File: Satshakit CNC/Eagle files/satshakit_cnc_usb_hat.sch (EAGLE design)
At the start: 30 parts

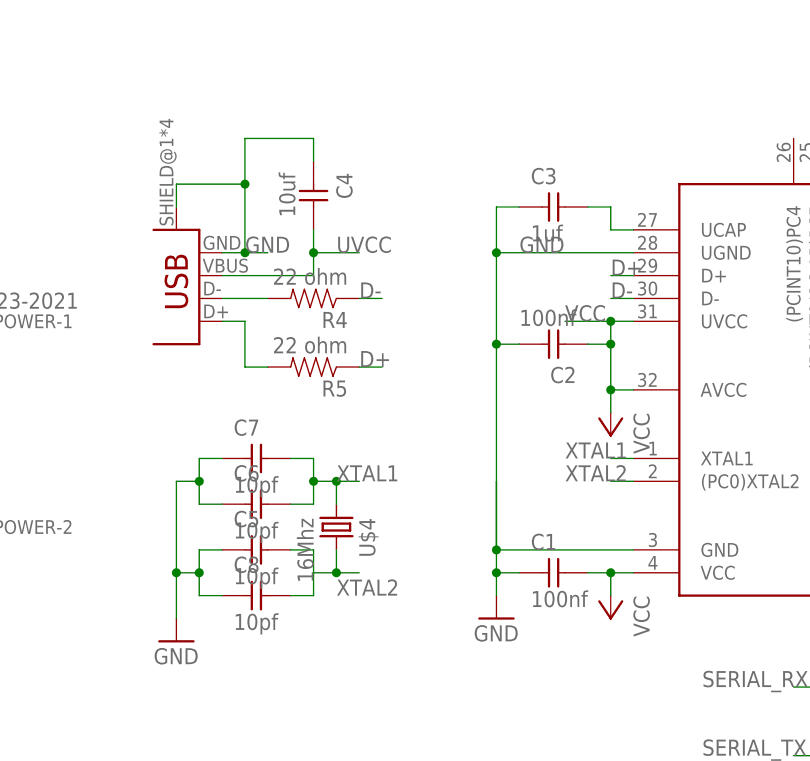
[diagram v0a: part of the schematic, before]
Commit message: New improved, simplified - yet to be properly testest - design. Most importantly it features a proper crystal trace and some elements redistribution
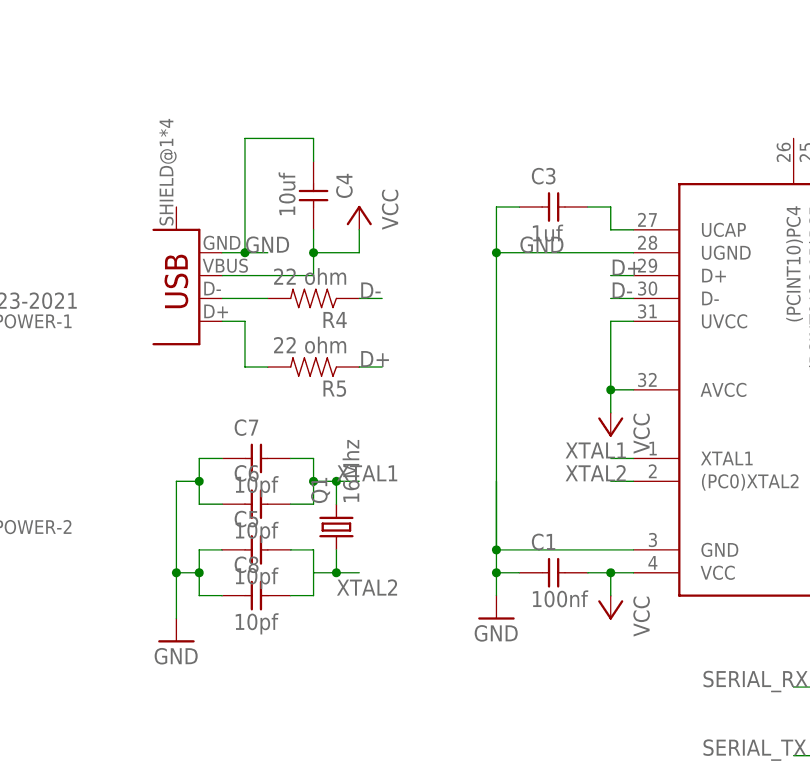
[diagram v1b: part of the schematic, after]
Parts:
- removed C2: 100nf, fab:CAP-UNPOLARIZEDFAB
- removed U$4: 16Mhz, fab:CRYSTAL
- added Q1: 16Mhz, crystal:CSM-7X-DU
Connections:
- removed net UVCC: C4.2, U$3.VBUS
- net GND: no longer C2.2, U$3.SHIELD
- net VCC: now also C4.2, U$3.VBUS; no longer C2.1
- net XTAL1: now also Q1.2; no longer U$4.1
- net XTAL2: now also Q1.1; no longer U$4.2
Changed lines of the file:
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@@
 <part name="C1" library="fab" deviceset="CAP-UNPOLARIZED" device="FAB" value="100nf"/>
 <part name="U$3" library="fab" deviceset="USB_MINIB" device=""/>
-<part name="C2" library="fab" deviceset="CAP-UNPOLARIZED" device="FAB" value="100nf"/>
 <part name="C3" library="fab" deviceset="CAP-UNPOLARIZED" device="FAB" value="1uf"/>
 <part name="GND1" library="supply1" library_urn="urn:adsk.eagle:library:371" deviceset="GND" device=""/>
@@
 <part name="R4" library="01_SparkFun" deviceset="RESISTOR" device="1206" value="22 ohm"/>
 <part name="R5" library="01_SparkFun" deviceset="RESISTOR" device="1206" value="22 ohm"/>
-<part name="U$4" library="fab" deviceset="CRYSTAL" device="" value="16Mhz"/>
 <part name="C8" library="fab" deviceset="CAP-UNPOLARIZED" device="FAB" value="10pf"/>
 <part name="C5" library="fab" deviceset="CAP-UNPOLARIZED" device="FAB" value="10pf"/>
@@
 <part name="R1" library="01_SparkFun" deviceset="RESISTOR" device="1206" value="1kohm"/>
 <part name="C9" library="fab" deviceset="CAP-UNPOLARIZED" device="FAB" value="100nf"/>
+<part name="P+2" library="supply1" library_urn="urn:adsk.eagle:library:371" deviceset="VCC" device=""/>
+<part name="Q1" library="crystal" library_urn="urn:adsk.eagle:library:204" deviceset="CSM-7X-DU" device="" package3d_urn="urn:adsk.eagle:package:12105/1" value="16Mhz"/>
 </parts>
 <sheets>
@@
 <instance part="C1" gate="&gt;NAME" x="20.32" y="40.64"/>
 <instance part="U$3" gate="G$1" x="-20.32" y="71.12" rot="R180"/>
-<instance part="C2" gate="&gt;NAME" x="17.78" y="66.04" rot="R180"/>
 <instance part="C3" gate="&gt;NAME" x="20.32" y="81.28"/>
 <instance part="GND1" gate="1" x="12.7" y="35.56"/>
@@
 <instance part="R4" gate="G$1" x="-7.62" y="71.12" rot="R180"/>
 <instance part="R5" gate="G$1" x="-7.62" y="63.5" rot="R180"/>
-<instance part="U$4" gate="G$1" x="-5.08" y="45.72" rot="R270"/>
 <instance part="C8" gate="&gt;NAME" x="-12.7" y="38.1"/>
 <instance part="C5" gate="&gt;NAME" x="-12.7" y="43.18"/>
@@
 <instance part="R1" gate="G$1" x="132.08" y="43.18" rot="R180"/>
 <instance part="C9" gate="&gt;NAME" x="132.08" y="50.8"/>
+<instance part="P+2" gate="VCC" x="-2.54" y="81.28" rot="MR0"/>
+<instance part="Q1" gate="P" x="-5.08" y="45.72" rot="R90"/>
 </instances>
 <busses>
@@
 </segment>
 <segment>
-<pinref part="U$1" gate="G$1" pin="AVCC"/>
-<wire x1="27.94" y1="60.96" x2="25.4" y2="60.96" width="0.1524" layer="91"/>
-<wire x1="25.4" y1="60.96" x2="25.4" y2="58.42" width="0.1524" layer="91"/>
-<pinref part="P+6" gate="VCC" pin="VCC"/>
-<pinref part="U$1" gate="G$1" pin="UVCC"/>
-<wire x1="27.94" y1="68.58" x2="25.4" y2="68.58" width="0.1524" layer="91"/>
-<wire x1="25.4" y1="68.58" x2="25.4" y2="66.04" width="0.1524" layer="91"/>
-<pinref part="C2" gate="&gt;NAME" pin="1"/>
-<wire x1="25.4" y1="66.04" x2="22.86" y2="66.04" width="0.1524" layer="91"/>
-<wire x1="25.4" y1="68.58" x2="20.32" y2="68.58" width="0.1524" layer="91"/>
-<junction x="25.4" y="68.58"/>
-<label x="20.32" y="68.58" size="1.778" layer="95"/>
-<wire x1="25.4" y1="66.04" x2="25.4" y2="60.96" width="0.1524" layer="91"/>
-<junction x="25.4" y="66.04"/>
-<junction x="25.4" y="60.96"/>
-</segment>
-<segment>
 <pinref part="U$2" gate="G$1" pin="VCC"/>
 <wire x1="137.16" y1="73.66" x2="142.24" y2="73.66" width="0.1524" layer="91"/>
@@
 <wire x1="66.04" y1="93.98" x2="66.04" y2="96.52" width="0.1524" layer="91"/>
 <pinref part="P+8" gate="VCC" pin="VCC"/>
+</segment>
+<segment>
+<pinref part="P+6" gate="VCC" pin="VCC"/>
+<wire x1="25.4" y1="58.42" x2="25.4" y2="60.96" width="0.1524" layer="91"/>
+<pinref part="U$1" gate="G$1" pin="AVCC"/>
+<wire x1="25.4" y1="60.96" x2="27.94" y2="60.96" width="0.1524" layer="91"/>
+<pinref part="U$1" gate="G$1" pin="UVCC"/>
+<wire x1="27.94" y1="68.58" x2="25.4" y2="68.58" width="0.1524" layer="91"/>
+<wire x1="25.4" y1="60.96" x2="25.4" y2="68.58" width="0.1524" layer="91"/>
+<junction x="25.4" y="60.96"/>
+</segment>
+<segment>
+<pinref part="U$3" gate="G$1" pin="VBUS"/>
+<wire x1="-17.78" y1="73.66" x2="-7.62" y2="73.66" width="0.1524" layer="91"/>
+<pinref part="C4" gate="&gt;NAME" pin="2"/>
+<wire x1="-7.62" y1="73.66" x2="-7.62" y2="76.2" width="0.1524" layer="91"/>
+<wire x1="-7.62" y1="76.2" x2="-7.62" y2="78.74" width="0.1524" layer="91"/>
+<junction x="-7.62" y="76.2"/>
+<wire x1="-7.62" y1="76.2" x2="-2.54" y2="76.2" width="0.1524" layer="91"/>
+<pinref part="P+2" gate="VCC" pin="VCC"/>
+<wire x1="-2.54" y1="78.74" x2="-2.54" y2="76.2" width="0.1524" layer="91"/>
 </segment>
 </net>
@@
 <wire x1="12.7" y1="50.8" x2="12.7" y2="43.18" width="0.1524" layer="91"/>
 <junction x="12.7" y="43.18"/>
-<pinref part="C2" gate="&gt;NAME" pin="2"/>
-<wire x1="15.24" y1="66.04" x2="12.7" y2="66.04" width="0.1524" layer="91"/>
 <pinref part="U$1" gate="G$1" pin="UGND"/>
 <wire x1="27.94" y1="76.2" x2="12.7" y2="76.2" width="0.1524" layer="91"/>
@@
 <label x="15.24" y="76.2" size="1.778" layer="95"/>
 <pinref part="C3" gate="&gt;NAME" pin="1"/>
-<wire x1="12.7" y1="76.2" x2="12.7" y2="66.04" width="0.1524" layer="91"/>
 <junction x="12.7" y="76.2"/>
-<junction x="12.7" y="66.04"/>
-<wire x1="12.7" y1="66.04" x2="12.7" y2="43.18" width="0.1524" layer="91"/>
+<wire x1="12.7" y1="76.2" x2="12.7" y2="43.18" width="0.1524" layer="91"/>
 </segment>
 <segment>
@@
 </segment>
 <segment>
-<pinref part="U$3" gate="G$1" pin="SHIELD"/>
-<wire x1="-22.86" y1="81.28" x2="-22.86" y2="83.82" width="0.1524" layer="91"/>
-<wire x1="-22.86" y1="83.82" x2="-15.24" y2="83.82" width="0.1524" layer="91"/>
-<wire x1="-15.24" y1="83.82" x2="-15.24" y2="76.2" width="0.1524" layer="91"/>
+<wire x1="-15.24" y1="88.9" x2="-15.24" y2="76.2" width="0.1524" layer="91"/>
 <pinref part="U$3" gate="G$1" pin="GND"/>
 <wire x1="-15.24" y1="76.2" x2="-17.78" y2="76.2" width="0.1524" layer="91"/>
@@
 <wire x1="-7.62" y1="86.36" x2="-7.62" y2="88.9" width="0.1524" layer="91"/>
 <wire x1="-7.62" y1="88.9" x2="-15.24" y2="88.9" width="0.1524" layer="91"/>
-<wire x1="-15.24" y1="88.9" x2="-15.24" y2="83.82" width="0.1524" layer="91"/>
-<junction x="-15.24" y="83.82"/>
 <label x="-15.24" y="76.2" size="1.778" layer="95"/>
 <wire x1="-15.24" y1="76.2" x2="-12.7" y2="76.2" width="0.1524" layer="91"/>
@@
 </segment>
 </net>
-<net name="UVCC" class="0">
-<segment>
-<pinref part="U$3" gate="G$1" pin="VBUS"/>
-<wire x1="-17.78" y1="73.66" x2="-7.62" y2="73.66" width="0.1524" layer="91"/>
-<pinref part="C4" gate="&gt;NAME" pin="2"/>
-<wire x1="-7.62" y1="73.66" x2="-7.62" y2="76.2" width="0.1524" layer="91"/>
-<label x="-5.08" y="76.2" size="1.778" layer="95"/>
-<wire x1="-7.62" y1="76.2" x2="-7.62" y2="78.74" width="0.1524" layer="91"/>
-<junction x="-7.62" y="76.2"/>
-<wire x1="-7.62" y1="76.2" x2="-2.54" y2="76.2" width="0.1524" layer="91"/>
-</segment>
-</net>
 <net name="N$4" class="0">
 <segment>
@@
 </segment>
 <segment>
-<pinref part="U$4" gate="G$1" pin="1"/>
 <wire x1="-5.08" y1="48.26" x2="-5.08" y2="50.8" width="0.1524" layer="91"/>
 <wire x1="-5.08" y1="50.8" x2="-2.54" y2="50.8" width="0.1524" layer="91"/>
@@
 <wire x1="-7.62" y1="48.26" x2="-7.62" y2="50.8" width="0.1524" layer="91"/>
 <junction x="-7.62" y="50.8"/>
+<pinref part="Q1" gate="P" pin="2"/>
 </segment>
 </net>
@@
 </segment>
 <segment>
-<pinref part="U$4" gate="G$1" pin="2"/>
 <wire x1="-5.08" y1="43.18" x2="-5.08" y2="40.64" width="0.1524" layer="91"/>
 <wire x1="-5.08" y1="40.64" x2="-2.54" y2="40.64" width="0.1524" layer="91"/>
@@
 <junction x="-5.08" y="40.64"/>
 <label x="-5.08" y="38.1" size="1.778" layer="95"/>
+<pinref part="Q1" gate="P" pin="1"/>
 </segment>
 </net>
@@
 will not be understood (or retained) with this version.
 </note>
+<note version="8.3" severity="warning">
+Since Version 8.3, EAGLE supports the association of 3D packages
+with devices in libraries, schematics, and board files. Those 3D
+packages will not be understood (or retained) with this version.
+</note>
 </compatibility>

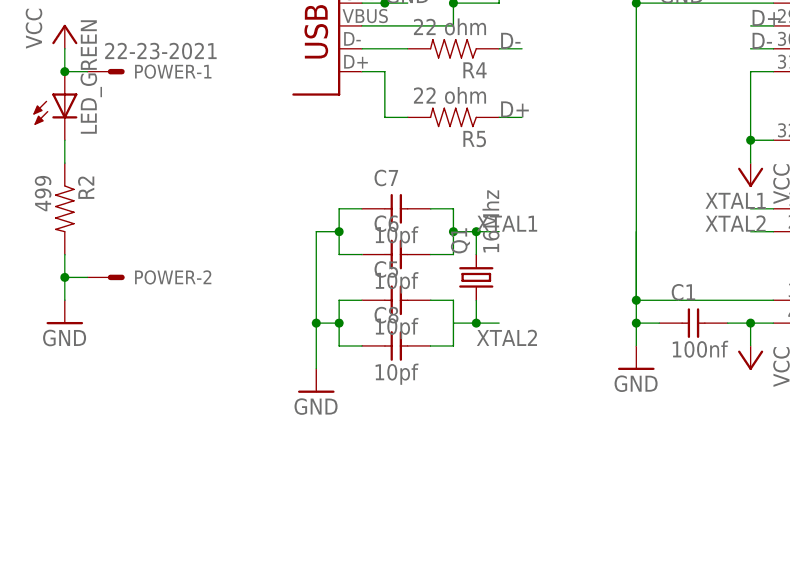
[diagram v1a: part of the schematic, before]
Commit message: Updated board. Reduced components and optimized traces. Added fancy writing
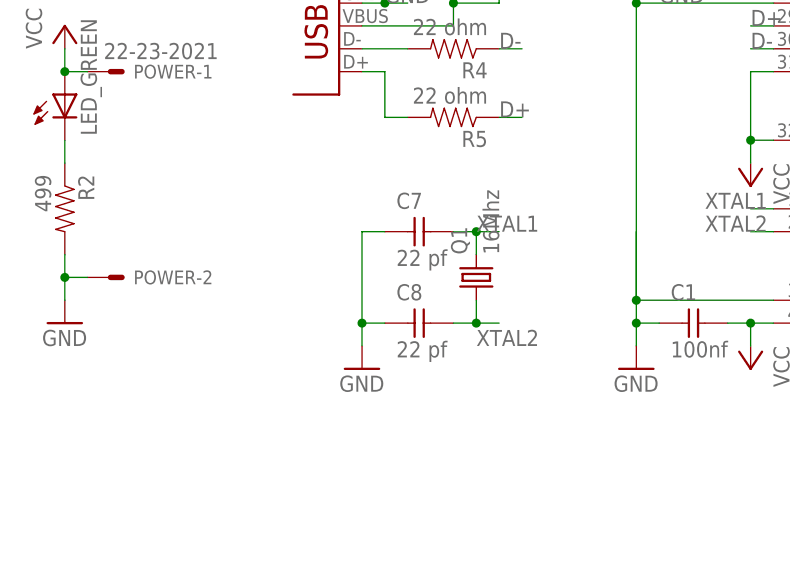
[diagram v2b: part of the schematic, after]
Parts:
- removed C5, C6: 10pf, fab:CAP-UNPOLARIZEDFAB
- C7, C8: value 10pf -> 22 pf
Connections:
- removed net N$3: C5.2, C8.2
- net GND: no longer C5.1, C6.1
- net XTAL1: no longer C6.2
- net XTAL2: now also C8.2
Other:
- moved on the sheet: C7, C8
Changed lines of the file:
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@@
 <part name="R4" library="01_SparkFun" deviceset="RESISTOR" device="1206" value="22 ohm"/>
 <part name="R5" library="01_SparkFun" deviceset="RESISTOR" device="1206" value="22 ohm"/>
-<part name="C8" library="fab" deviceset="CAP-UNPOLARIZED" device="FAB" value="10pf"/>
-<part name="C5" library="fab" deviceset="CAP-UNPOLARIZED" device="FAB" value="10pf"/>
-<part name="C6" library="fab" deviceset="CAP-UNPOLARIZED" device="FAB" value="10pf"/>
-<part name="C7" library="fab" deviceset="CAP-UNPOLARIZED" device="FAB" value="10pf"/>
+<part name="C8" library="fab" deviceset="CAP-UNPOLARIZED" device="FAB" value="22 pf"/>
+<part name="C7" library="fab" deviceset="CAP-UNPOLARIZED" device="FAB" value="22 pf"/>
 <part name="GND6" library="supply1" library_urn="urn:adsk.eagle:library:371" deviceset="GND" device=""/>
 <part name="GND7" library="supply1" library_urn="urn:adsk.eagle:library:371" deviceset="GND" device=""/>
@@
 <instance part="R4" gate="G$1" x="-7.62" y="71.12" rot="R180"/>
 <instance part="R5" gate="G$1" x="-7.62" y="63.5" rot="R180"/>
-<instance part="C8" gate="&gt;NAME" x="-12.7" y="38.1"/>
-<instance part="C5" gate="&gt;NAME" x="-12.7" y="43.18"/>
-<instance part="C6" gate="&gt;NAME" x="-12.7" y="48.26"/>
-<instance part="C7" gate="&gt;NAME" x="-12.7" y="53.34"/>
-<instance part="GND6" gate="1" x="-22.86" y="33.02"/>
+<instance part="C8" gate="&gt;NAME" x="-10.16" y="40.64"/>
+<instance part="C7" gate="&gt;NAME" x="-10.16" y="50.8"/>
+<instance part="GND6" gate="1" x="-17.78" y="35.56"/>
 <instance part="GND7" gate="1" x="-50.8" y="40.64"/>
 <instance part="P+7" gate="VCC" x="-50.8" y="73.66"/>
@@
 </segment>
 <segment>
-<pinref part="C7" gate="&gt;NAME" pin="1"/>
-<wire x1="-17.78" y1="53.34" x2="-20.32" y2="53.34" width="0.1524" layer="91"/>
-<pinref part="C6" gate="&gt;NAME" pin="1"/>
-<wire x1="-20.32" y1="53.34" x2="-20.32" y2="50.8" width="0.1524" layer="91"/>
-<wire x1="-20.32" y1="50.8" x2="-20.32" y2="48.26" width="0.1524" layer="91"/>
-<wire x1="-20.32" y1="48.26" x2="-17.78" y2="48.26" width="0.1524" layer="91"/>
-<wire x1="-20.32" y1="50.8" x2="-22.86" y2="50.8" width="0.1524" layer="91"/>
-<junction x="-20.32" y="50.8"/>
-<wire x1="-22.86" y1="50.8" x2="-22.86" y2="40.64" width="0.1524" layer="91"/>
-<pinref part="C5" gate="&gt;NAME" pin="1"/>
-<wire x1="-17.78" y1="43.18" x2="-20.32" y2="43.18" width="0.1524" layer="91"/>
-<pinref part="C8" gate="&gt;NAME" pin="1"/>
-<wire x1="-20.32" y1="43.18" x2="-20.32" y2="40.64" width="0.1524" layer="91"/>
-<wire x1="-20.32" y1="40.64" x2="-20.32" y2="38.1" width="0.1524" layer="91"/>
-<wire x1="-20.32" y1="38.1" x2="-17.78" y2="38.1" width="0.1524" layer="91"/>
-<wire x1="-22.86" y1="40.64" x2="-20.32" y2="40.64" width="0.1524" layer="91"/>
-<junction x="-20.32" y="40.64"/>
-<wire x1="-22.86" y1="40.64" x2="-22.86" y2="35.56" width="0.1524" layer="91"/>
-<junction x="-22.86" y="40.64"/>
-<pinref part="GND6" gate="1" pin="GND"/>
-</segment>
-<segment>
 <pinref part="U$2" gate="G$1" pin="GND"/>
 <wire x1="137.16" y1="68.58" x2="142.24" y2="68.58" width="0.1524" layer="91"/>
@@
 <wire x1="139.7" y1="43.18" x2="137.16" y2="43.18" width="0.1524" layer="91"/>
 </segment>
+<segment>
+<pinref part="C8" gate="&gt;NAME" pin="1"/>
+<pinref part="GND6" gate="1" pin="GND"/>
+<wire x1="-15.24" y1="40.64" x2="-17.78" y2="40.64" width="0.1524" layer="91"/>
+<wire x1="-17.78" y1="40.64" x2="-17.78" y2="38.1" width="0.1524" layer="91"/>
+<pinref part="C7" gate="&gt;NAME" pin="1"/>
+<wire x1="-15.24" y1="50.8" x2="-17.78" y2="50.8" width="0.1524" layer="91"/>
+<wire x1="-17.78" y1="50.8" x2="-17.78" y2="40.64" width="0.1524" layer="91"/>
+<junction x="-17.78" y="40.64"/>
+</segment>
 </net>
 <net name="N$26" class="0">
@@
 <wire x1="-5.08" y1="48.26" x2="-5.08" y2="50.8" width="0.1524" layer="91"/>
 <wire x1="-5.08" y1="50.8" x2="-2.54" y2="50.8" width="0.1524" layer="91"/>
-<wire x1="-5.08" y1="50.8" x2="-7.62" y2="50.8" width="0.1524" layer="91"/>
+<label x="-5.08" y="50.8" size="1.778" layer="95"/>
+<pinref part="Q1" gate="P" pin="2"/>
+<pinref part="C7" gate="&gt;NAME" pin="2"/>
+<wire x1="-7.62" y1="50.8" x2="-5.08" y2="50.8" width="0.1524" layer="91"/>
 <junction x="-5.08" y="50.8"/>
-<label x="-5.08" y="50.8" size="1.778" layer="95"/>
-<pinref part="C7" gate="&gt;NAME" pin="2"/>
-<wire x1="-10.16" y1="53.34" x2="-7.62" y2="53.34" width="0.1524" layer="91"/>
-<wire x1="-7.62" y1="53.34" x2="-7.62" y2="50.8" width="0.1524" layer="91"/>
-<pinref part="C6" gate="&gt;NAME" pin="2"/>
-<wire x1="-10.16" y1="48.26" x2="-7.62" y2="48.26" width="0.1524" layer="91"/>
-<wire x1="-7.62" y1="48.26" x2="-7.62" y2="50.8" width="0.1524" layer="91"/>
-<junction x="-7.62" y="50.8"/>
-<pinref part="Q1" gate="P" pin="2"/>
 </segment>
 </net>
@@
 <wire x1="-5.08" y1="43.18" x2="-5.08" y2="40.64" width="0.1524" layer="91"/>
 <wire x1="-5.08" y1="40.64" x2="-2.54" y2="40.64" width="0.1524" layer="91"/>
+<label x="-5.08" y="38.1" size="1.778" layer="95"/>
+<pinref part="Q1" gate="P" pin="1"/>
+<pinref part="C8" gate="&gt;NAME" pin="2"/>
 <wire x1="-5.08" y1="40.64" x2="-7.62" y2="40.64" width="0.1524" layer="91"/>
 <junction x="-5.08" y="40.64"/>
-<label x="-5.08" y="38.1" size="1.778" layer="95"/>
-<pinref part="Q1" gate="P" pin="1"/>
 </segment>
 </net>
@@
 </segment>
 </net>
-<net name="N$3" class="0">
-<segment>
-<pinref part="C5" gate="&gt;NAME" pin="2"/>
-<wire x1="-10.16" y1="43.18" x2="-7.62" y2="43.18" width="0.1524" layer="91"/>
-<wire x1="-7.62" y1="43.18" x2="-7.62" y2="38.1" width="0.1524" layer="91"/>
-<pinref part="C8" gate="&gt;NAME" pin="2"/>
-<wire x1="-7.62" y1="38.1" x2="-10.16" y2="38.1" width="0.1524" layer="91"/>
-</segment>
-</net>
